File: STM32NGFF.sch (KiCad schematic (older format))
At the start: 27 parts, among them J1 2199119-4, P1 CX70M-24P1, U1 STM32F303CCTx, U2 USBLC6-2SC6, Y1 16MHz

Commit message: added github repo to schematic and PCB
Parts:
- added C?: 10uf, symbol Device:C_Small
- added C?: 11uf, symbol Device:C_Small
- added C?: 100uf, symbol Device:C_Small
- added R?: 121, symbol Device:R_Small
- added RV?: 1k, symbol Device:Varistor
- added U?: LM1117-3.3, symbol Regulator_Linear:LM1117-3.3
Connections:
- wire segments 100 -> 121
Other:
- note added: "5V to 3.3V Conversion Using LM117"
- note added: "Original 5V to 3.3V Conversion"
- note removed: "5V to 3.3V Conversion (BAD, NEEDS UPDATE)"
- moved on the sheet: C1, C2, C3, C4, C5, C6, C7, C8, C9, D1, D2, H1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

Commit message: Updated to built-in USB symbol and organized schematic
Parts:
- removed P1: CX70M-24P1, symbol CX70M-24P1:CX70M-24P1
- removed R1: 2k, symbol Device:R_Small
- removed R2: 1k, symbol Device:R_Small
- added J?: USB_C_Receptacle_USB2.0, symbol Connector:USB_C_Receptacle_USB2.0
- gave numbers to parts that had none: 6
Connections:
- wire segments 121 -> 114
- no-connect marks 9 -> 0
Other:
- note added: "TODO:\n-------\n1. Design electrical circuits (in progress)\n2. Choose Components\n3. Select/obtain/create footprints\n4. Create rough PCB layout\n5. Refine PCB Layout\n6. Order prototype\n7. Validate prototype, make PCB adjustments\n8. Order beta samples\n9. Beta test\n10. ....\n11. No profit. In this for the love of the game."
- note removed: "Original 5V to 3.3V Conversion"
- note removed: "TODO:\n1. Design electrical circuits\n2. Choose Components\n3. Select/obtain/create footprints\n4. Create rough PCB layout\n5. Refine PCB Layout\n6. Order prototype\n7. Validate prototype, make PCB adjustments\n8. Order beta samples\n9. Beta test\n10. ....\n11. No profit. In this for the love of the game."
- moved on the sheet: C1, C2, C3, C4, C5, C6, C7, H1, J1, L1, R10, R9

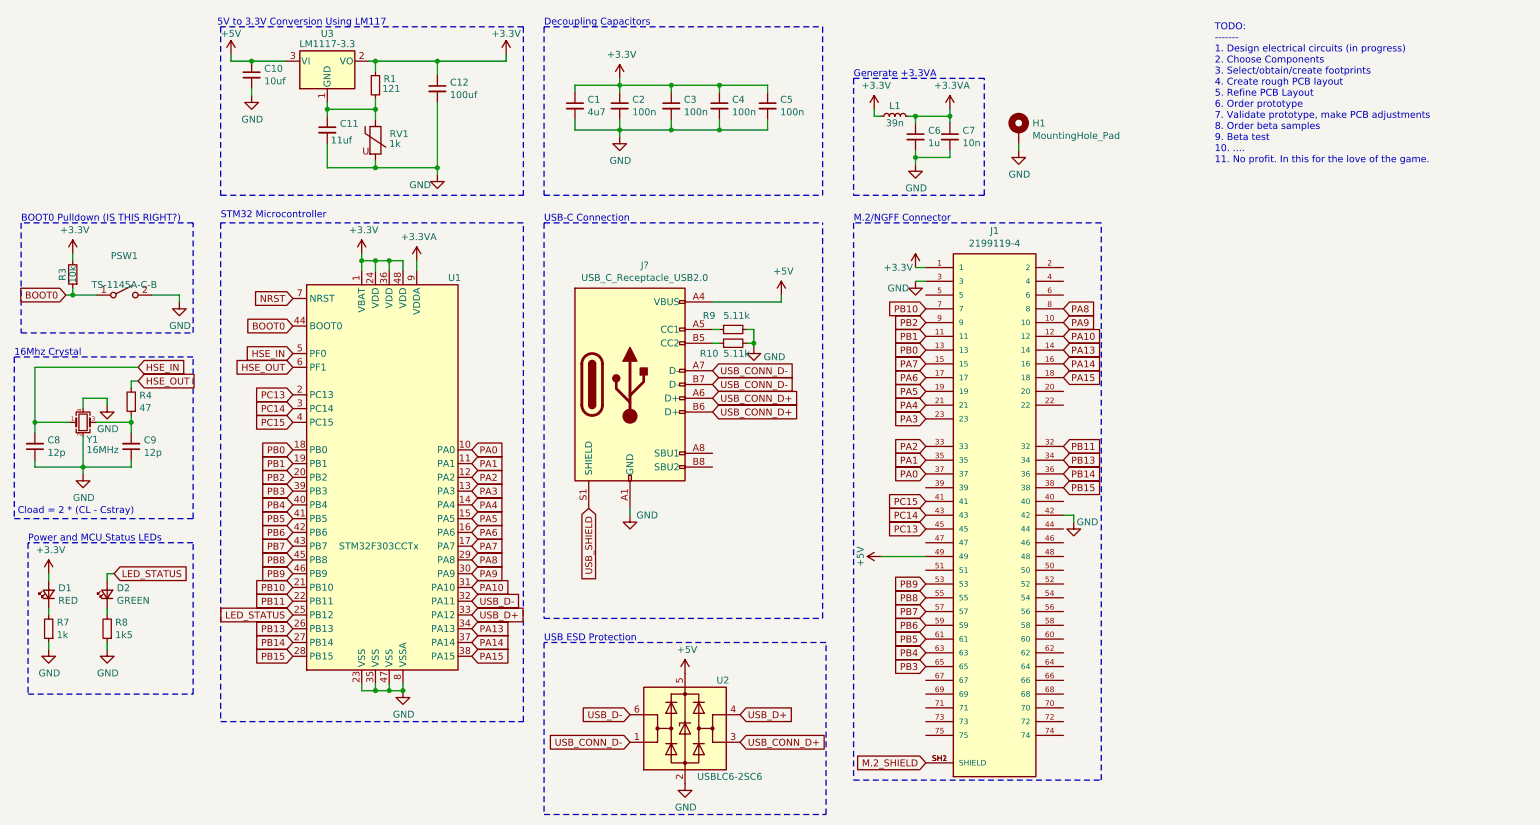
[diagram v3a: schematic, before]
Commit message: Removed blank PCB and updated schematic with Discord info
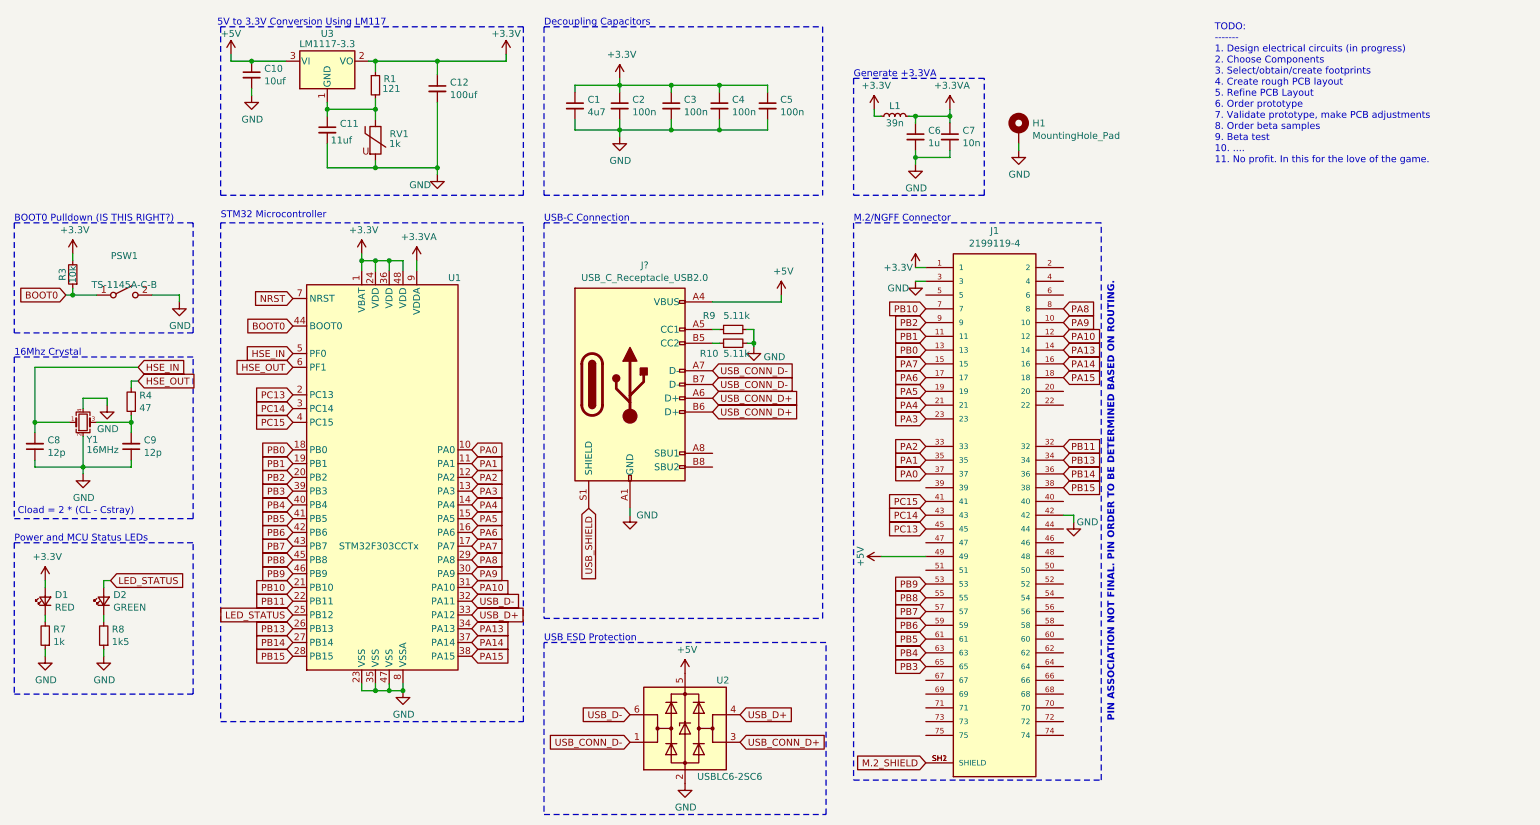
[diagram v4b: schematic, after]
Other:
- note added: "PIN ASSOCIATION NOT FINAL. PIN ORDER TO BE DETERMINED BASED ON ROUTING."
- moved on the sheet: D1, D2, R7, R8
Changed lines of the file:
@@
 Rev "0.1"
 Comp "Open Source Hardware, GNU GPL v3.0 Or Later"
-Comment1 "https://github.com/cyberknet/STM32NGFF"
+Comment1 "Latest version at https://github.com/cyberknet/STM32NGFF"
 Comment2 ""
-Comment3 ""
-Comment4 ""
+Comment3 "Join us on Discord at https://discord.gg/E6ujkUG"
+Comment4 "Created by the members of 33C (fka reindeer pig baboon with mouse accessory)"
 $EndDescr
 Wire Wire Line
@@
 L Device:LED_Small D2
 U 1 1 5FFA3B6D
-P 1250 4700
-F 0 "D2" V 1296 4630 50  0000 R CNN
-F 1 "GREEN" V 1205 4630 50  0000 R CNN
-F 2 "" V 1250 4700 50  0001 C CNN
-F 3 "~" V 1250 4700 50  0001 C CNN
-	1    1250 4700
+P 1225 4750
+F 0 "D2" V 1271 4680 50  0000 R CNN
+F 1 "GREEN" V 1180 4680 50  0000 R CNN
+F 2 "" V 1225 4750 50  0001 C CNN
+F 3 "~" V 1225 4750 50  0001 C CNN
+	1    1225 4750
 	0    -1   -1   0
 $EndComp
-Text GLabel 1300 4550 2    50   Input ~ 0
+Text GLabel 1275 4600 2    50   Input ~ 0
 LED_STATUS
 Wire Wire Line
-	1250 4550 1250 4600
+	1225 4600 1225 4650
 $Comp
 L Device:R_Small R8
 U 1 1 5FFAA498
-P 1250 4950
-F 0 "R8" H 1191 4904 50  0000 R CNN
-F 1 "1k5" H 1191 4995 50  0000 R CNN
-F 2 "" H 1250 4950 50  0001 C CNN
-F 3 "~" H 1250 4950 50  0001 C CNN
-	1    1250 4950
+P 1225 5000
+F 0 "R8" H 1166 4954 50  0000 R CNN
+F 1 "1k5" H 1166 5045 50  0000 R CNN
+F 2 "" H 1225 5000 50  0001 C CNN
+F 3 "~" H 1225 5000 50  0001 C CNN
+	1    1225 5000
 	-1   0    0    1
 $EndComp
 Wire Wire Line
-	1250 4800 1250 4850
+	1225 4850 1225 4900
 $Comp
 L power:GND #PWR025
 U 1 1 5FFAD17C
-P 1250 5100
-F 0 "#PWR025" H 1250 4850 50  0001 C CNN
-F 1 "GND" H 1255 4927 50  0000 C CNN
-F 2 "" H 1250 5100 50  0001 C CNN
-F 3 "" H 1250 5100 50  0001 C CNN
-	1    1250 5100
-	1    0    0    -1
-$EndComp
-Wire Wire Line
-	1250 5050 1250 5100
+P 1225 5150
+F 0 "#PWR025" H 1225 4900 50  0001 C CNN
+F 1 "GND" H 1230 4977 50  0000 C CNN
+F 2 "" H 1225 5150 50  0001 C CNN
+F 3 "" H 1225 5150 50  0001 C CNN
+	1    1225 5150
+	1    0    0    -1
+$EndComp
+Wire Wire Line
+	1225 5100 1225 5150
 $Comp
 L Power_Protection:USBLC6-2SC6 U2
@@
 L Device:LED_Small D1
 U 1 1 601B9F45
-P 825 4700
-F 0 "D1" V 871 4630 50  0000 R CNN
-F 1 "RED" V 780 4630 50  0000 R CNN
-F 2 "" V 825 4700 50  0001 C CNN
-F 3 "~" V 825 4700 50  0001 C CNN
-	1    825  4700
+P 800 4750
+F 0 "D1" V 846 4680 50  0000 R CNN
+F 1 "RED" V 755 4680 50  0000 R CNN
+F 2 "" V 800 4750 50  0001 C CNN
+F 3 "~" V 800 4750 50  0001 C CNN
+	1    800  4750
 	0    -1   -1   0
 $EndComp
@@
 L power:+3.3V #PWR021
 U 1 1 601BB184
-P 825 4550
-F 0 "#PWR021" H 825 4400 50  0001 C CNN
-F 1 "+3.3V" H 840 4723 50  0000 C CNN
-F 2 "" H 825 4550 50  0001 C CNN
-F 3 "" H 825 4550 50  0001 C CNN
-	1    825  4550
-	1    0    0    -1
-$EndComp
-Wire Wire Line
-	825  4550 825  4600
+P 800 4600
+F 0 "#PWR021" H 800 4450 50  0001 C CNN
+F 1 "+3.3V" H 815 4773 50  0000 C CNN
+F 2 "" H 800 4600 50  0001 C CNN
+F 3 "" H 800 4600 50  0001 C CNN
+	1    800  4600
+	1    0    0    -1
+$EndComp
+Wire Wire Line
+	800  4600 800  4650
 $Comp
 L Device:R_Small R7
 U 1 1 601C2629
-P 825 4950
-F 0 "R7" H 766 4904 50  0000 R CNN
-F 1 "1k" H 766 4995 50  0000 R CNN
-F 2 "" H 825 4950 50  0001 C CNN
-F 3 "~" H 825 4950 50  0001 C CNN
-	1    825  4950
+P 800 5000
+F 0 "R7" H 741 4954 50  0000 R CNN
+F 1 "1k" H 741 5045 50  0000 R CNN
+F 2 "" H 800 5000 50  0001 C CNN
+F 3 "~" H 800 5000 50  0001 C CNN
+	1    800  5000
 	-1   0    0    1
 $EndComp
 Wire Wire Line
-	825  4800 825  4850
+	800  4850 800  4900
 $Comp
 L power:GND #PWR022
 U 1 1 601C9D6A
-P 825 5100
-F 0 "#PWR022" H 825 4850 50  0001 C CNN
-F 1 "GND" H 830 4927 50  0000 C CNN
-F 2 "" H 825 5100 50  0001 C CNN
-F 3 "" H 825 5100 50  0001 C CNN
-	1    825  5100
-	1    0    0    -1
-$EndComp
-Wire Wire Line
-	825  5050 825  5100
+P 800 5150
+F 0 "#PWR022" H 800 4900 50  0001 C CNN
+F 1 "GND" H 805 4977 50  0000 C CNN
+F 2 "" H 800 5150 50  0001 C CNN
+F 3 "" H 800 5150 50  0001 C CNN
+	1    800  5150
+	1    0    0    -1
+$EndComp
+Wire Wire Line
+	800  5100 800  5150
 $Comp
 L Mechanical:MountingHole_Pad H1
@@
 M.2_SHIELD
 Wire Wire Line
-	1250 4550 1300 4550
-Wire Notes Line
-	675  4325 675  5425
-Wire Notes Line
-	675  5425 1875 5425
+	1225 4600 1275 4600
+Wire Notes Line
+	575  4325 575  5425
 Wire Notes Line
 	1875 5425 1875 4325
-Wire Notes Line
-	1875 4325 675  4325
-Text Notes 675  4325 0    50   ~ 0
+Text Notes 575  4325 0    50   ~ 0
 Power and MCU Status LEDs
 Wire Notes Line
@@
 Generate +3.3VA
 Wire Notes Line
-	625  2000 625  2800
-Wire Notes Line
-	625  2800 1875 2800
+	575  2000 575  2800
 Wire Notes Line
 	1875 2800 1875 2000
-Wire Notes Line
-	1875 2000 625  2000
-Text Notes 625  2000 0    50   ~ 0
+Text Notes 575  2000 0    50   ~ 0
 BOOT0 Pulldown (IS THIS RIGHT?)
 Wire Notes Line
@@
 Wire Notes Line
 	4425 575  4425 1800
+Wire Notes Line
+	575  4325 1875 4325
+Wire Notes Line
+	575  5425 1875 5425
+Wire Notes Line
+	575  2000 1875 2000
+Wire Notes Line
+	575  2800 1875 2800
+Text Notes 8575 2425 3    50   ~ 10
+PIN ASSOCIATION NOT FINAL. PIN ORDER TO BE DETERMINED BASED ON ROUTING.
 $EndSCHEMATC

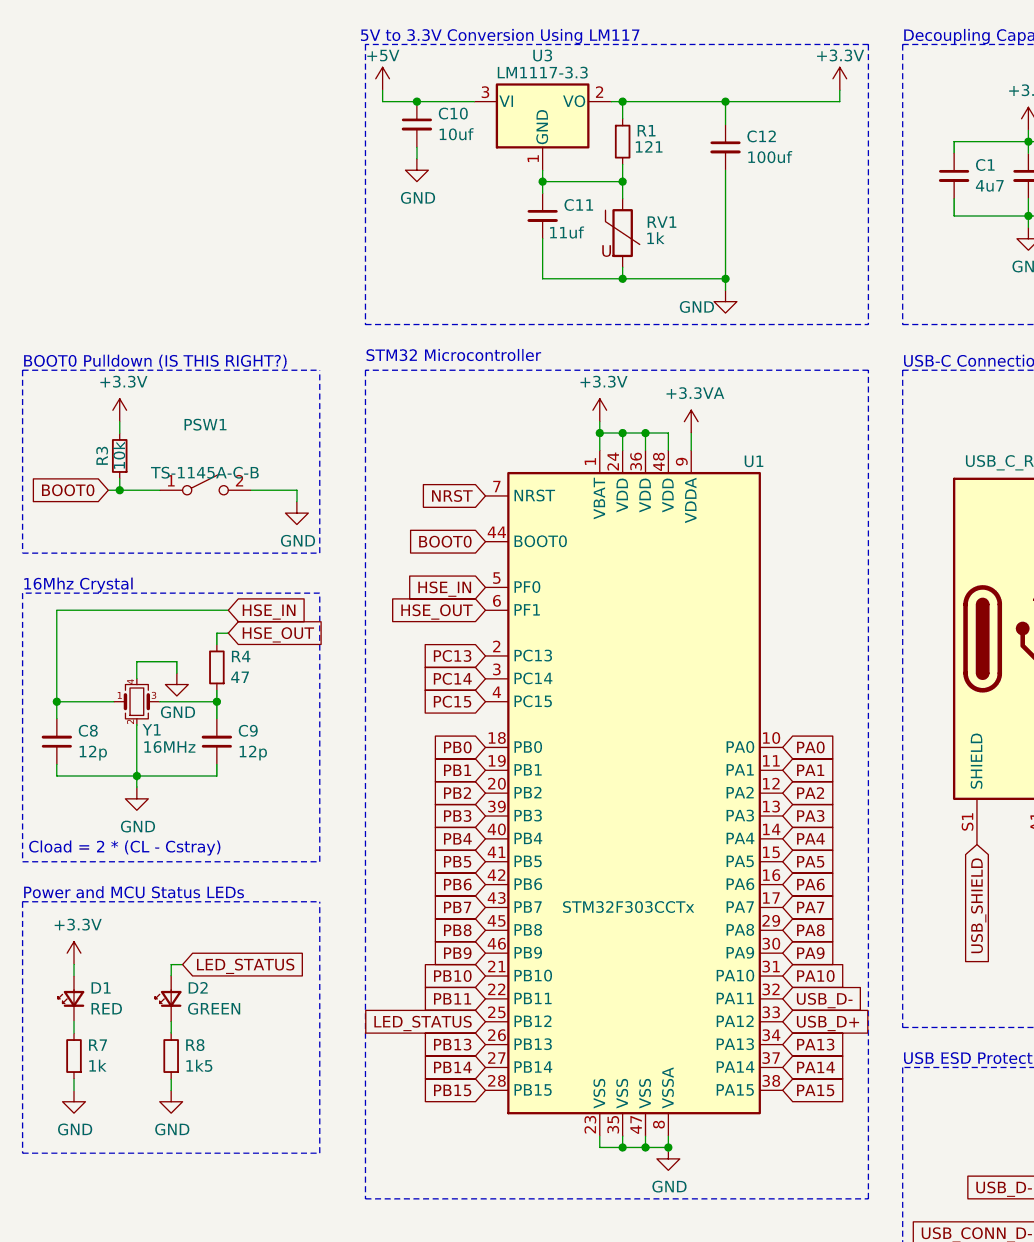
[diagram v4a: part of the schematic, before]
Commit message: Updated 3.3V generation to MIC5205
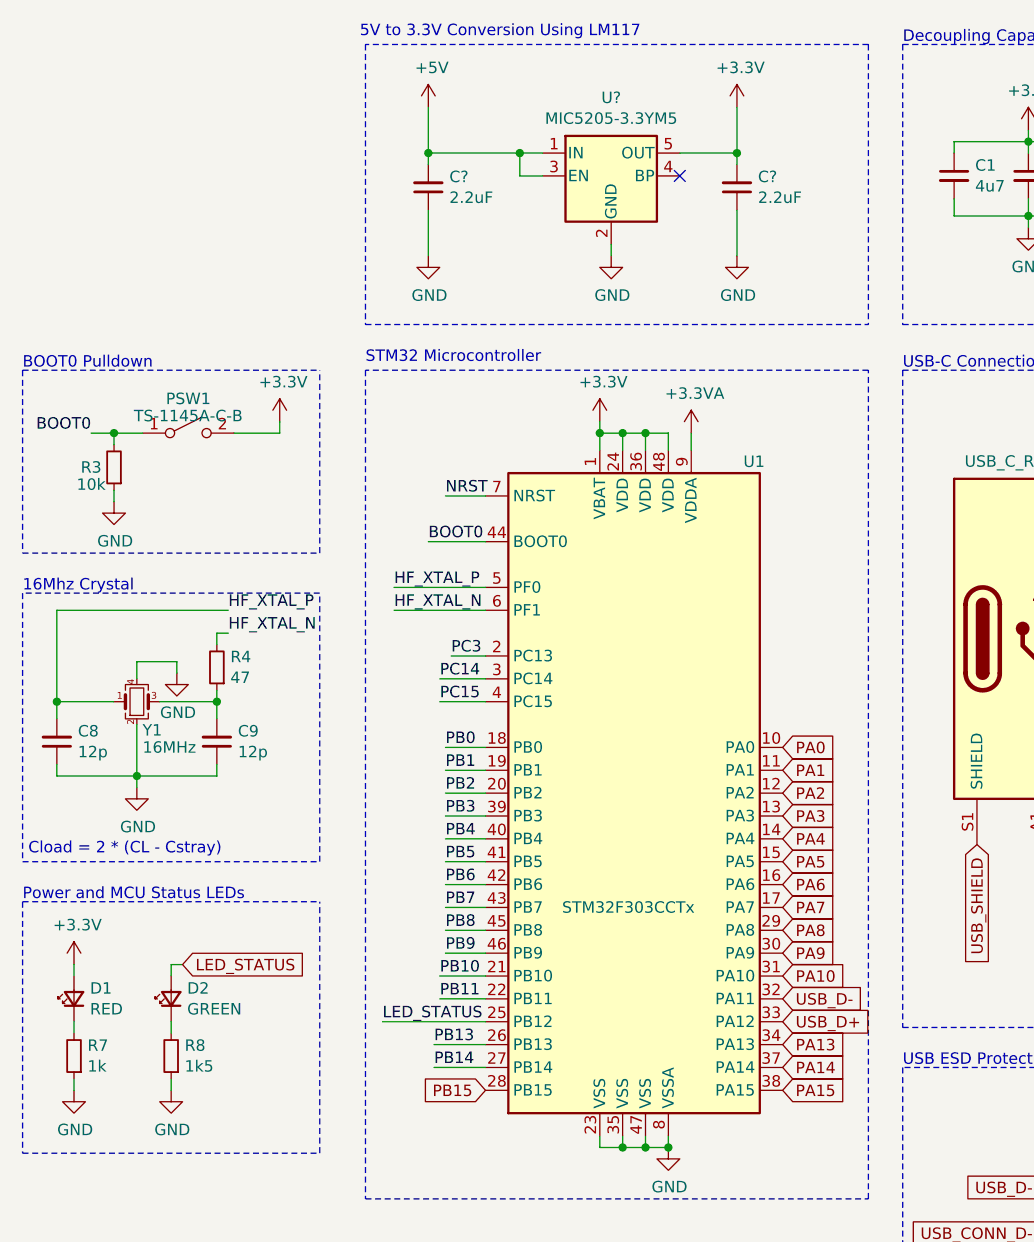
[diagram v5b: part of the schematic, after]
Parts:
- removed C10: 10uf, symbol Device:C_Small
- removed C11: 11uf, symbol Device:C_Small
- removed C12: 100uf, symbol Device:C_Small
- removed R1: 121, symbol Device:R_Small
- removed RV1: 1k, symbol Device:Varistor
- removed U3: LM1117-3.3, symbol Regulator_Linear:LM1117-3.3
- added C? (x2): 2.2uF, symbol Device:C_Small
- added U?: MIC5205-3.3YM5, Package_TO_SOT_SMD:SOT-23-5, symbol Regulator_Linear:MIC5205-3.3YM5
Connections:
- net +3V3: now also PSW1.2 (B), C?.2, U?.5 (OUT); no longer R3.2
- net +5V: now also C?.2, U?.1 (IN), U?.3 (EN)
- net BOOT0: now also R3.2; no longer R3.1
- net GND: now also R3.1, C?.1, C?.1, U?.2 (GND); no longer PSW1.2 (B)
- net PC13: no longer U1.2 (PC13)
- net HSE_IN renamed HF_XTAL_P
- net HSE_OUT renamed HF_XTAL_N
- new net PC3: U1.2 (PC13)
- no-connect marks 0 -> 1
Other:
- note added: "BOOT0 Pulldown"
- note removed: "BOOT0 Pulldown (IS THIS RIGHT?)"
- moved on the sheet: PSW1, R3
